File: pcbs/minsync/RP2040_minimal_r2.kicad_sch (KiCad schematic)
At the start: 36 parts, among them J1 SWD_CONN, J2 Comm, J4 Comm, J5 Comm, J6 Comm, SW1 SW_Push, U1 NCP1117-3.3_SOT223, U2 W25Q128JVS, U3 RP2040, U4 Si5351A-B-GT, Y2 Crystal_GND24

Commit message: Update minsync PCB
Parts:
- removed TP1, TP2, TP3: TestPoint, TestPoint:TestPoint_Keystone_5019_Minature, symbol Connector:TestPoint
- added D1, D2: LED, LED_SMD:LED_0603_1608Metric, symbol Device:LED
- added J3: Conn_01x01_Pin, Connector_PinHeader_1.27mm:PinHeader_1x01_P1.27mm_Vertical, symbol Connector:Conn_01x01_Pin
- added R3, R4: 470R, Resistor_SMD:R_0402_1005Metric, symbol Device:R
- SW1: footprint (none) -> Button_Switch_SMD:SW_Push_SPST_NO_Alps_SKRK
- TP1: renamed from TP4; footprint TestPoint:TestPoint_Keystone_5019_Minature -> Connector_PinHeader_2.54mm:PinHeader_1x01_P2.54mm_Vertical
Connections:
- net GND: now also D1.1 (K), D2.1 (K)
- net GPIO28_ADC2: now also R3.2
- net GPIO29_ADC3: now also R4.2
- net RUN: now also J3.1 (Pin_1)
- new net: D2.2 (A), R4.1
- new net: D1.2 (A), R3.1
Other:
- note added: "Clocks"
- note removed: "Crystal"
- moved on the sheet: TP1

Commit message: Add BOM and CPL of minsync v0.1
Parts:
- J2: LCSC (none) -> C225520
- SW1: footprint Button_Switch_SMD:SW_Push_SPST_NO_Alps_SKRK -> RP2040_minimal:TS-1187A-PushButton; LCSC (none) -> C72443
- U1: LCSC (none) -> C154606
- U2: LCSC (none) -> C97521
- U3: LCSC (none) -> C2040
- U4: LCSC (none) -> C504891
- Y2: LCSC (none) -> C1985619
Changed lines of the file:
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@@
 			)
 		)
+		(property "LCSC" "C2040"
+			(at 198.12 144.78 0)
+			(effects
+				(font
+					(size 1.27 1.27)
+				)
+				(hide yes)
+			)
+		)
 		(pin "1"
 		)
@@
 			)
 		)
+		(property "LCSC" "C97521"
+			(at 97.79 133.35 0)
+			(effects
+				(font
+					(size 1.27 1.27)
+				)
+				(hide yes)
+			)
+		)
 		(pin "1"
 		)
@@
 			)
 		)
+		(property "LCSC" "C154606"
+			(at 76.2 44.45 0)
+			(effects
+				(font
+					(size 1.27 1.27)
+				)
+				(hide yes)
+			)
+		)
 		(pin "1"
 		)
@@
 			)
 		)
-		(property "Footprint" "Button_Switch_SMD:SW_Push_SPST_NO_Alps_SKRK"
+		(property "Footprint" "RP2040_minimal:TS-1187A-PushButton"
 			(at 26.67 120.65 0)
 			(effects
@@
 			)
 		)
+		(property "LCSC" "C72443"
+			(at 26.67 125.73 0)
+			(effects
+				(font
+					(size 1.27 1.27)
+				)
+				(hide yes)
+			)
+		)
 		(pin "1"
 		)
@@
 			)
 		)
+		(property "LCSC" "C225520"
+			(at 350.52 31.75 0)
+			(effects
+				(font
+					(size 1.27 1.27)
+				)
+				(hide yes)
+			)
+		)
 		(pin "9"
 		)
@@
 			)
 		)
+		(property "LCSC" "C504891"
+			(at 87.63 234.95 0)
+			(effects
+				(font
+					(size 1.27 1.27)
+				)
+				(hide yes)
+			)
+		)
 		(pin "9"
 		)
@@
 			(at 50.8 227.33 0)
 			(effects
+				(font
+					(size 1.27 1.27)
+				)
+				(hide yes)
+			)
+		)
+		(property "LCSC" "C1985619"
+			(at 50.8 227.33 0)
+			(effects

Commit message: Clock experiments
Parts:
- added J8: SSD1306, Connector_PinHeader_2.54mm:PinHeader_1x04_P2.54mm_Vertical, symbol Connector:Conn_01x04_Pin
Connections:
- net +3V3: now also J8.3 (Pin_3)
- net GND: now also J8.4 (Pin_4)
- net GPIO28_ADC2: now also J8.1 (Pin_1)
- net GPIO29_ADC3: now also J8.2 (Pin_2)
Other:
- note added: "TODO: check BOOTSEL button: compare to RPi Pico check if screen would actually fit"

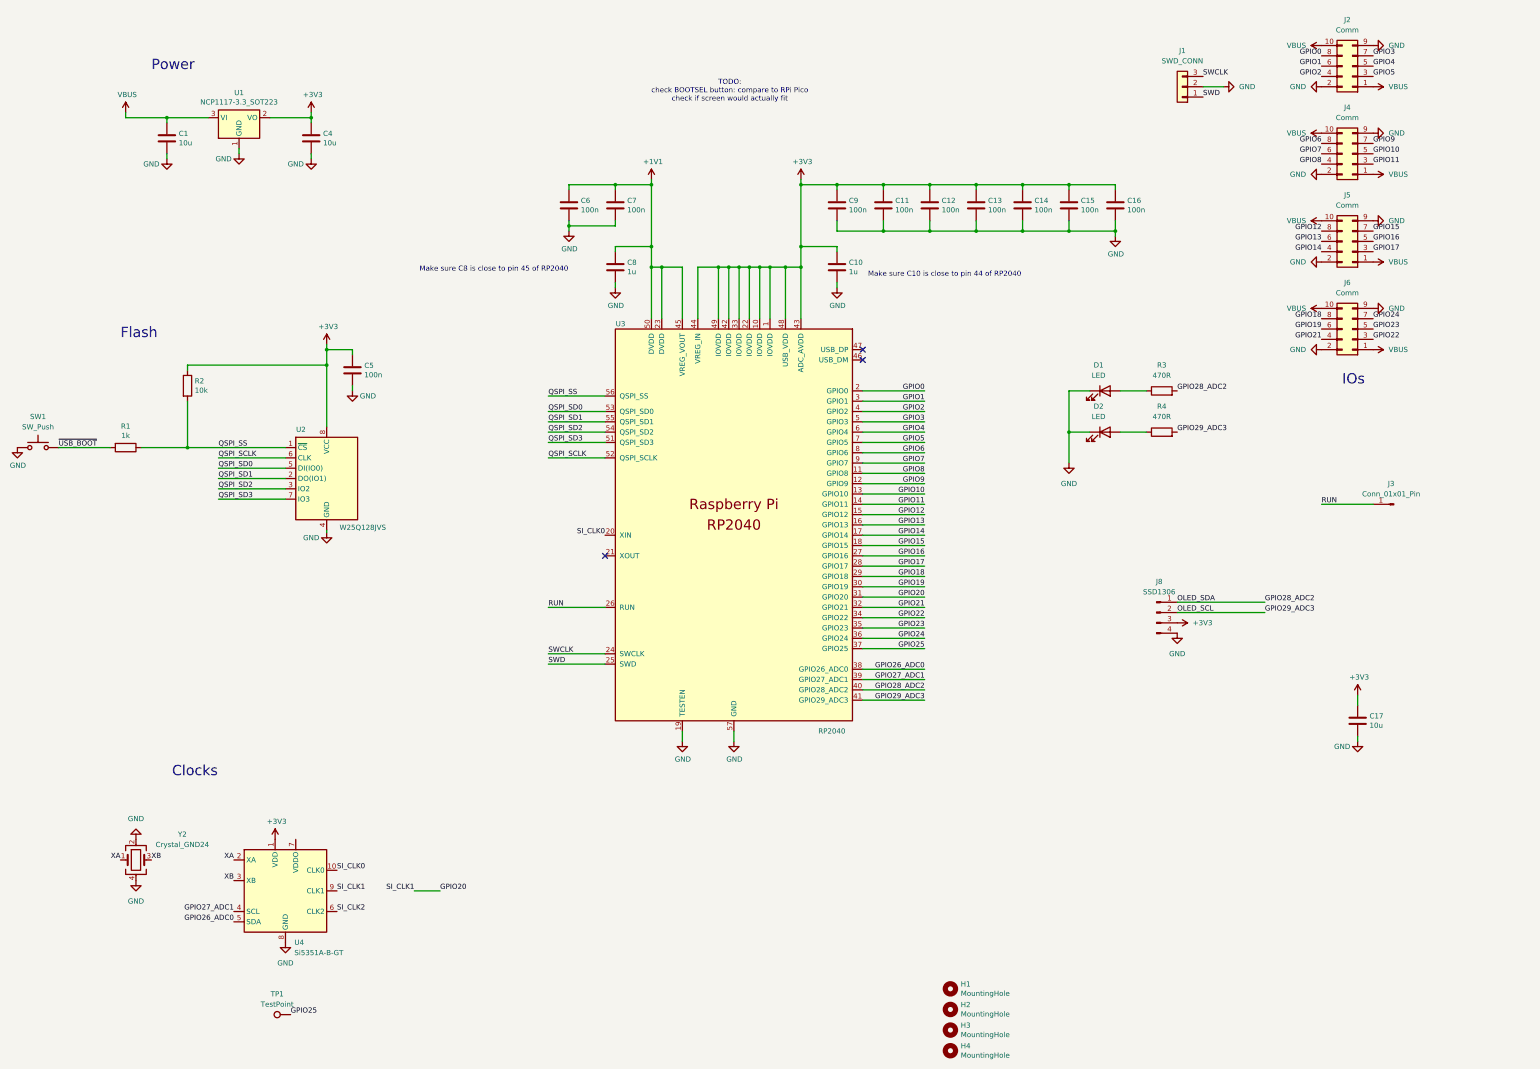
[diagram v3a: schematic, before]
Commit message: Switch to 2x4P headers
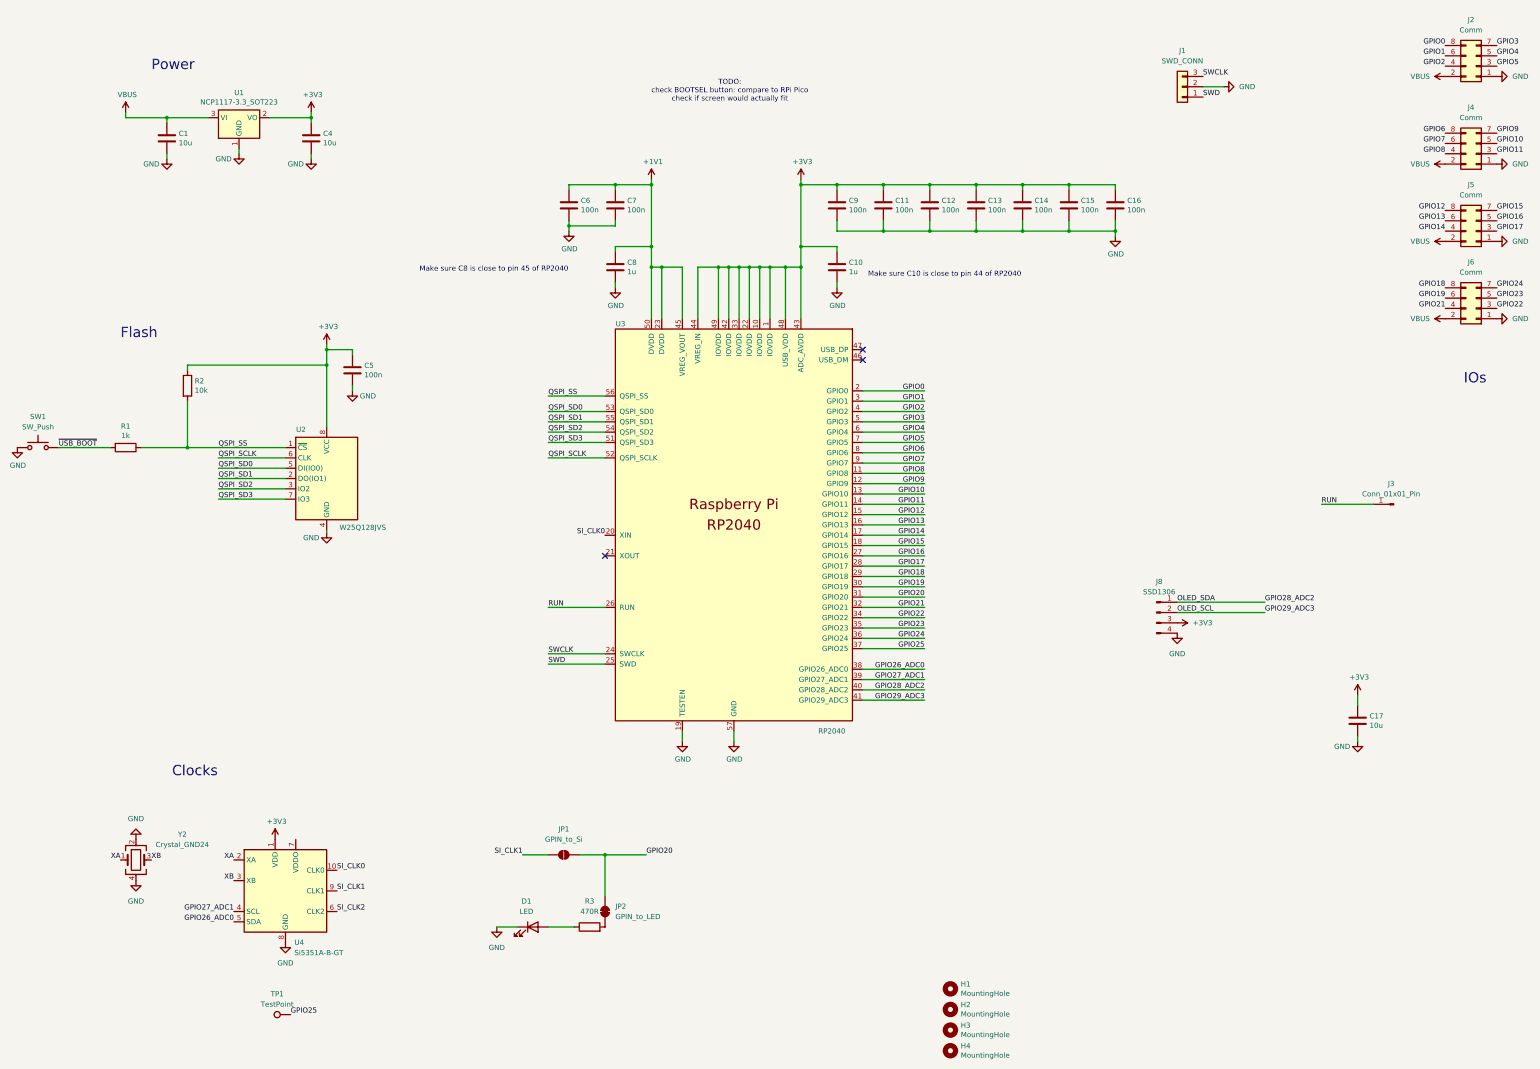
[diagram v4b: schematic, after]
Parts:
- removed D2: LED, LED_SMD:LED_0603_1608Metric, symbol Device:LED
- removed J2, J4, J5, J6: Comm, Connector_PinHeader_2.54mm:PinHeader_2x05_P2.54mm_Vertical, symbol Connector_Generic:Conn_02x05_Odd_Even
- removed R4: 470R, Resistor_SMD:R_0402_1005Metric, symbol Device:R
- added J2, J4, J5, J6: Comm, Connector_PinHeader_2.54mm:PinHeader_2x04_P2.54mm_Vertical, symbol Connector_Generic:Conn_02x04_Odd_Even
- added JP1: GPIN_to_Si, Jumper:SolderJumper-2_P1.3mm_Open_RoundedPad1.0x1.5mm, symbol Jumper:SolderJumper_2_Open
- added JP2: GPIN_to_LED, Jumper:SolderJumper-2_P1.3mm_Bridged_RoundedPad1.0x1.5mm, symbol Jumper:SolderJumper_2_Bridged
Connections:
- net GND: now also J2.1 (Pin_1), J4.1 (Pin_1), J5.1 (Pin_1), J6.1 (Pin_1)
- net GPIO0: now also J2.8 (Pin_8)
- net GPIO1: now also J2.6 (Pin_6)
- net GPIO10: now also J4.5 (Pin_5)
- net GPIO11: now also J4.3 (Pin_3)
- net GPIO12: now also J5.8 (Pin_8)
- net GPIO13: now also J5.6 (Pin_6)
- net GPIO14: now also J5.4 (Pin_4)
- net GPIO15: now also J5.7 (Pin_7)
- net GPIO16: now also J5.5 (Pin_5)
- net GPIO17: now also J5.3 (Pin_3)
- net GPIO18: now also J6.8 (Pin_8)
- net GPIO19: now also J6.6 (Pin_6)
- net GPIO2: now also J2.4 (Pin_4)
- net GPIO20: now also JP1.2 (B), JP2.2 (B); no longer U4.9 (CLK1)
- net GPIO21: now also J6.4 (Pin_4)
- net GPIO22: now also J6.3 (Pin_3)
- net GPIO23: now also J6.5 (Pin_5)
- net GPIO24: now also J6.7 (Pin_7)
- net GPIO28_ADC2: no longer R3.2
- net GPIO3: now also J2.7 (Pin_7)
- net GPIO4: now also J2.5 (Pin_5)
- net GPIO5: now also J2.3 (Pin_3)
- net GPIO6: now also J4.8 (Pin_8)
- net GPIO7: now also J4.6 (Pin_6)
- net GPIO8: now also J4.4 (Pin_4)
- net GPIO9: now also J4.7 (Pin_7)
- net VBUS: now also J2.2 (Pin_2), J4.2 (Pin_2), J5.2 (Pin_2), J6.2 (Pin_2)
- new net: JP2.1 (A), R3.2
- new net SI_CLK1: JP1.1 (A), U4.9 (CLK1)
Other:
- moved on the sheet: D1, R3

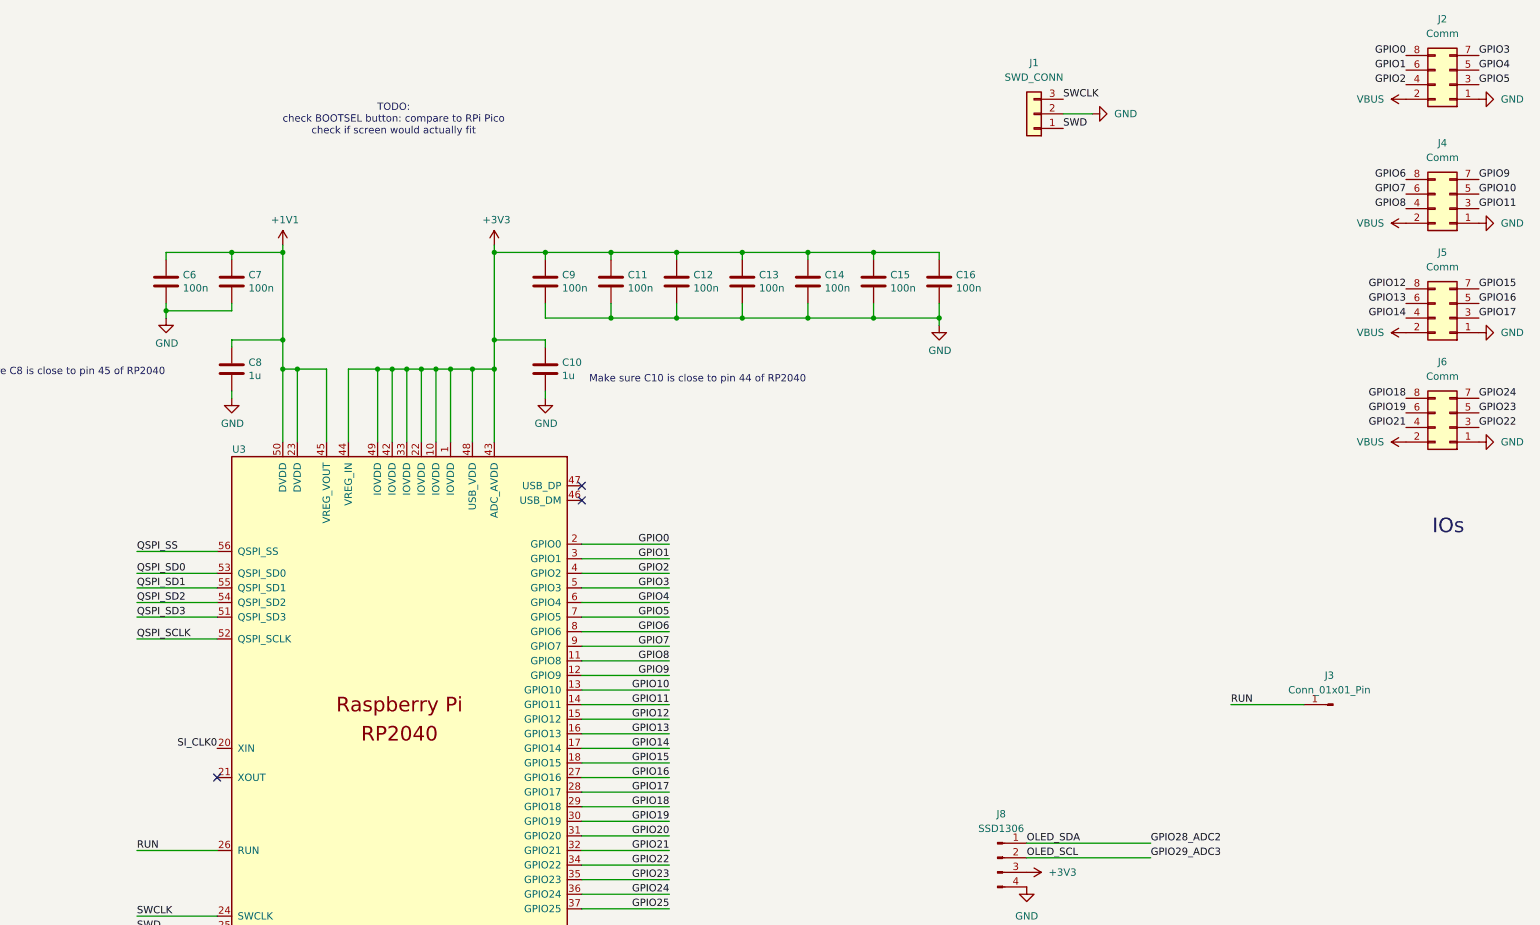
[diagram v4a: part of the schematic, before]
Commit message: Use 2x4P headers for connectors
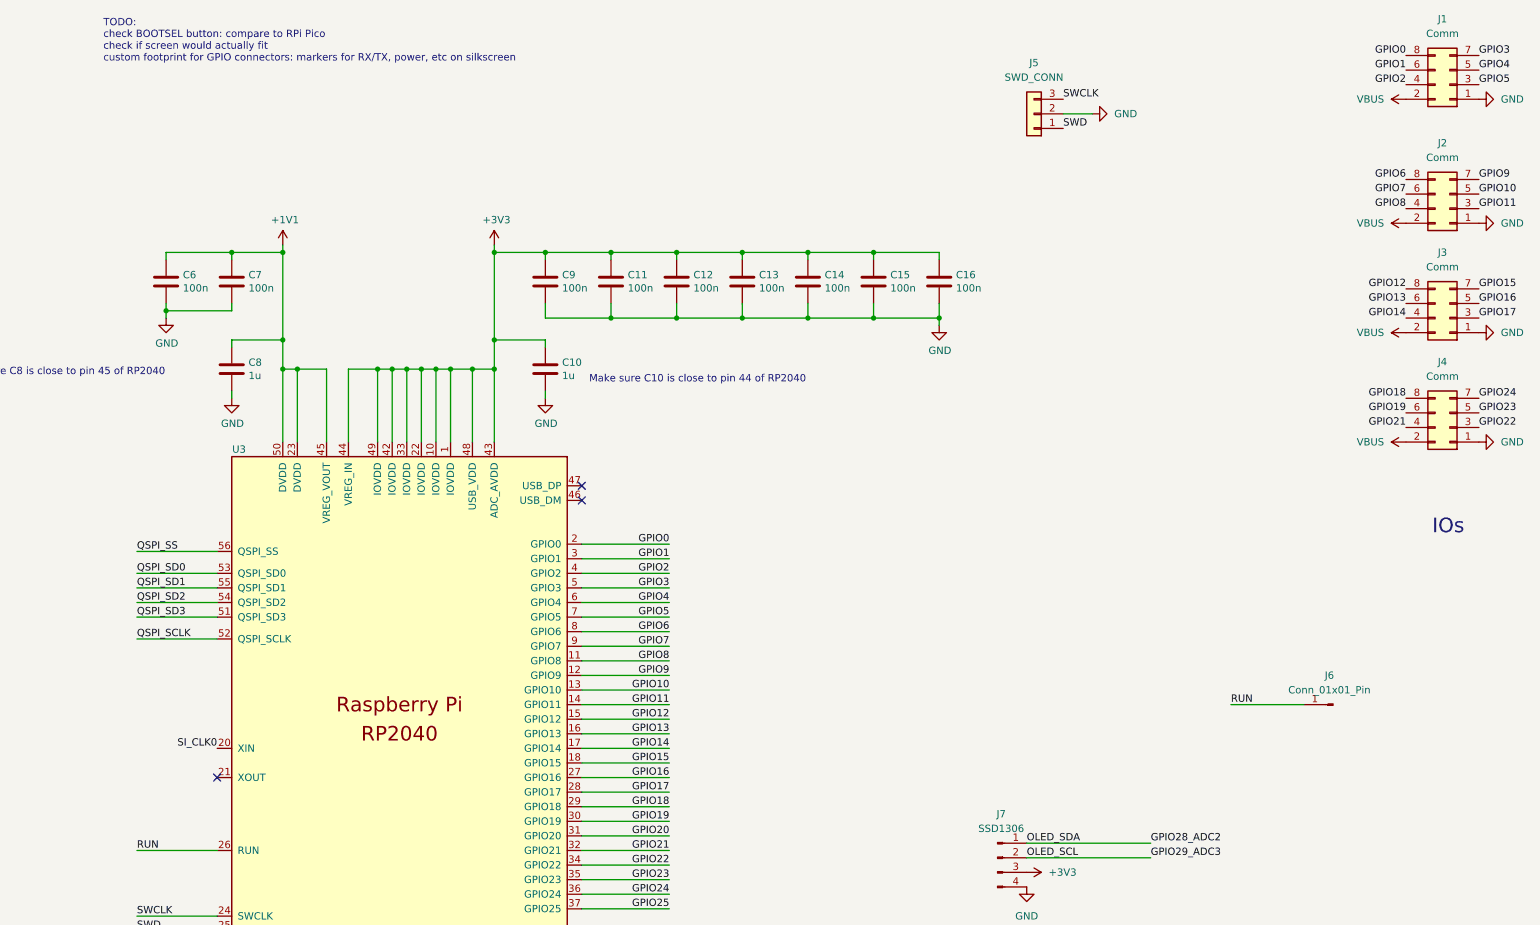
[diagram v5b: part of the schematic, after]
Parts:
- renumbered J2 to J1, J4 to J2, J5 to J3, J6 to J4, J1 to J5, J3 to J6, J8 to J7
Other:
- note added: "TODO: check BOOTSEL button: compare to RPi Pico check if screen would actually fit custom footprint for GPIO connectors: markers for RX/TX, power, etc on silkscreen"
- note removed: "TODO: check BOOTSEL button: compare to RPi Pico check if screen would actually fit"
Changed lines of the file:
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@@
 		)
 	)
-	(text "TODO:\ncheck BOOTSEL button: compare to RPi Pico\ncheck if screen would actually fit"
+	(text "TODO:\ncheck BOOTSEL button: compare to RPi Pico\ncheck if screen would actually fit\ncustom footprint for GPIO connectors: markers for RX/TX, power, etc on silkscreen"
 		(exclude_from_sim no)
-		(at 197.104 37.846 0)
+		(at 146.558 24.13 0)
 		(effects
 			(font
 				(size 1.27 1.27)
 			)
+			(justify left)
 		)
 	)
@@
 		(dnp no)
 		(fields_autoplaced yes)
-		(property "Reference" "J6"
+		(property "Reference" "J4"
 			(at 379.73 80.01 0)
 			(effects
@@
 			(project "RP2040_minimal_r2"
 				(path "/8c0b3d8b-46d3-4173-ab1e-a61765f77d61"
-					(reference "J6")
+					(reference "J4")
 					(unit 1)
 				)
@@
 		(dnp no)
 		(fields_autoplaced yes)
-		(property "Reference" "J8"
+		(property "Reference" "J7"
 			(at 302.895 158.75 0)
 			(effects
@@
 			(project ""
 				(path "/8c0b3d8b-46d3-4173-ab1e-a61765f77d61"
-					(reference "J8")
+					(reference "J7")
 					(unit 1)
 				)
@@
 		(dnp no)
 		(fields_autoplaced yes)
-		(property "Reference" "J3"
+		(property "Reference" "J6"
 			(at 360.045 134.62 0)
 			(effects
@@
 			(project ""
 				(path "/8c0b3d8b-46d3-4173-ab1e-a61765f77d61"
-					(reference "J3")
+					(reference "J6")
 					(unit 1)
 				)
@@
 		(dnp no)
 		(fields_autoplaced yes)
-		(property "Reference" "J1"
+		(property "Reference" "J5"
 			(at 308.61 27.94 0)
 			(effects
@@
 			(project ""
 				(path "/8c0b3d8b-46d3-4173-ab1e-a61765f77d61"
-					(reference "J1")
+					(reference "J5")
 					(unit 1)
 				)
@@
 		(dnp no)
 		(fields_autoplaced yes)
-		(property "Reference" "J5"
+		(property "Reference" "J3"
 			(at 379.73 60.96 0)
 			(effects
@@
 			(project "RP2040_minimal_r2"
 				(path "/8c0b3d8b-46d3-4173-ab1e-a61765f77d61"
-					(reference "J5")
+					(reference "J3")
 					(unit 1)
 				)
@@
 		(dnp no)
 		(fields_autoplaced yes)
-		(property "Reference" "J2"
+		(property "Reference" "J1"
 			(at 379.73 20.32 0)
 			(effects
@@
 			(project ""
 				(path "/8c0b3d8b-46d3-4173-ab1e-a61765f77d61"
-					(reference "J2")
+					(reference "J1")
 					(unit 1)
 				)
@@
 		(dnp no)
 		(fields_autoplaced yes)
-		(property "Reference" "J4"
+		(property "Reference" "J2"
 			(at 379.73 41.91 0)
 			(effects
@@
 			(project "RP2040_minimal_r2"
 				(path "/8c0b3d8b-46d3-4173-ab1e-a61765f77d61"
-					(reference "J4")
+					(reference "J2")
 					(unit 1)
 				)

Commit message: Implement minsync_connect v0.1
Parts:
- J1, J2, J3, J4: footprint Connector_PinHeader_2.54mm:PinHeader_2x04_P2.54mm_Vertical -> RP2040_minimal:pitopi_and_power
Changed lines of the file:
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@@
 			)
 		)
-		(property "Footprint" "Connector_PinHeader_2.54mm:PinHeader_2x04_P2.54mm_Vertical"
+		(property "Footprint" "RP2040_minimal:pitopi_and_power"
 			(at 381 91.44 0)
 			(effects
@@
 			)
 		)
-		(property "Footprint" "Connector_PinHeader_2.54mm:PinHeader_2x04_P2.54mm_Vertical"
+		(property "Footprint" "RP2040_minimal:pitopi_and_power"
 			(at 381 72.39 0)
 			(effects
@@
 			)
 		)
-		(property "Footprint" "Connector_PinHeader_2.54mm:PinHeader_2x04_P2.54mm_Vertical"
+		(property "Footprint" "RP2040_minimal:pitopi_and_power"
 			(at 381 31.75 0)
 			(effects
@@
 			)
 		)
-		(property "Footprint" "Connector_PinHeader_2.54mm:PinHeader_2x04_P2.54mm_Vertical"
+		(property "Footprint" "RP2040_minimal:pitopi_and_power"
 			(at 381 53.34 0)
 			(effects

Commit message: Dry run ordering minsync and minsync connect v0.1
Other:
- note added: "TODO: x check BOOTSEL button: compare to RPi Pico check if screen would actually fit x check RUN pin with rp minimal"
- note removed: "TODO: check BOOTSEL button: compare to RPi Pico check if screen would actually fit custom footprint for GPIO connectors: markers for RX/TX, power, etc on silkscreen"
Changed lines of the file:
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@@
 		)
 	)
-	(text "TODO:\ncheck BOOTSEL button: compare to RPi Pico\ncheck if screen would actually fit\ncustom footprint for GPIO connectors: markers for RX/TX, power, etc on silkscreen"
+	(text "TODO:\nx check BOOTSEL button: compare to RPi Pico\ncheck if screen would actually fit\nx check RUN pin with rp minimal"
 		(exclude_from_sim no)
 		(at 146.558 24.13 0)
